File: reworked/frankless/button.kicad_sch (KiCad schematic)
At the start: 1 part

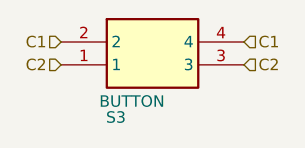
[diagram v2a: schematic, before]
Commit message: Fix reset and boot button.
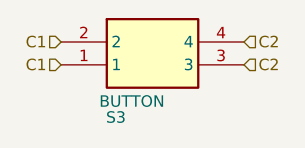
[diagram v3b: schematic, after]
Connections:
- net C1: now also S3.1; no longer S3.4
- net C2: now also S3.4; no longer S3.1
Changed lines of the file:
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@@
 		(comment 1 "https://github.com/arlaneenalra/pi-pico-boards/tree/main/reworked/frankless")
 	)
-	(hierarchical_label "C2"
+	(hierarchical_label "C1"
 		(shape input)
 		(at 146.05 99.06 180)
@@
 		)
 	)
-	(hierarchical_label "C1"
+	(hierarchical_label "C2"
 		(shape input)
 		(at 166.37 96.52 0)
